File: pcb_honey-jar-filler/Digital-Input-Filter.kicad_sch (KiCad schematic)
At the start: 3 parts

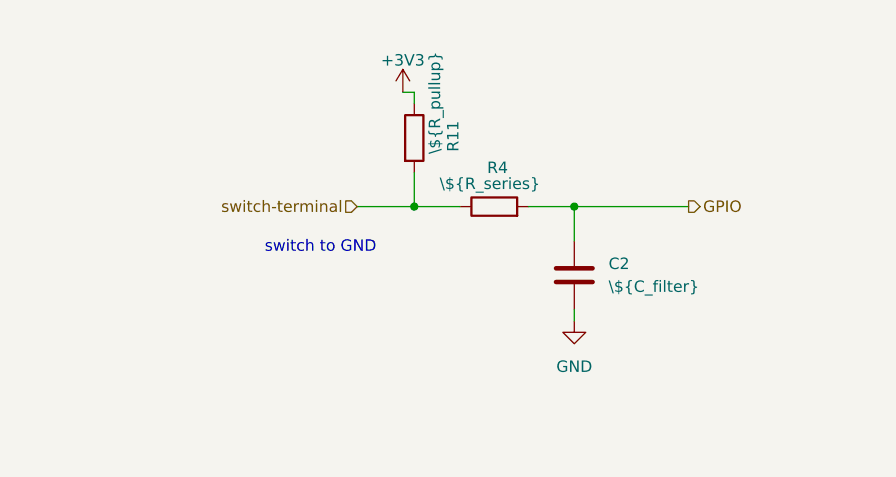
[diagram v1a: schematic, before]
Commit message: PCB: Optimize schematic layout, Add thesis schematic version
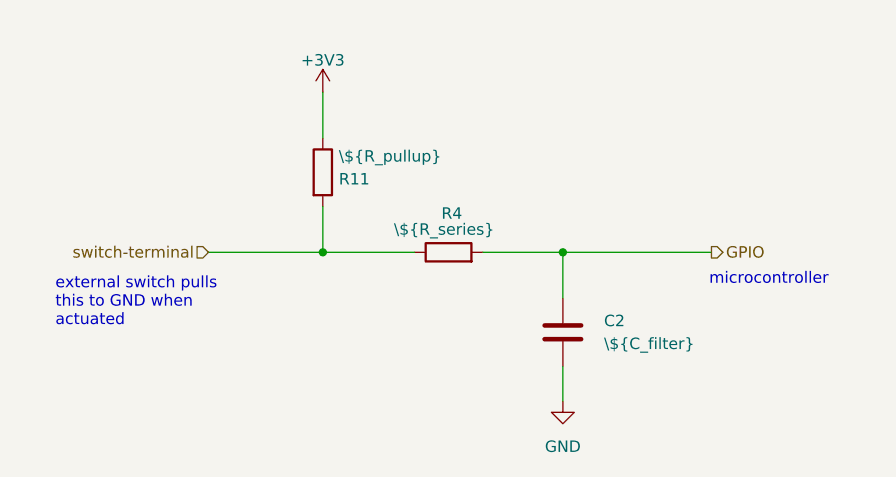
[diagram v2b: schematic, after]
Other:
- note added: "external switch pulls this to GND when actuated"
- note added: "microcontroller"
- note removed: "switch to GND"
- title: (none) -> Digital-Input-Filter
- moved on the sheet: C2, R11, R4
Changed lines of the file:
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@@
 	(generator "eeschema")
 	(generator_version "10.0")
-	(paper "A4")
-	(text "switch to GND"
-		(exclude_from_sim no)
-		(at 54.356 41.402 0)
+	(paper "A5")
+	(title_block
+		(title "Digital-Input-Filter")
+		(comment 1 "schematic component re-used for multiple inputs")
+	)
+	(text "microcontroller"
+		(exclude_from_sim no)
+		(at 97.536 44.958 0)
 		(effects
 			(font
 				(size 1.27 1.27)
 			)
-		)
-	)
-	(junction
-		(at 64.77 36.83)
-		(diameter 0)
-		(color 0 0 0 0)
-	)
-	(junction
-		(at 82.55 36.83)
-		(diameter 0)
-		(color 0 0 0 0)
-	)
-	(wire
-		(pts
-			(xy 58.42 36.83) (xy 64.77 36.83)
-		)
-		(stroke
-			(width 0)
-			(type default)
-		)
-	)
-	(wire
-		(pts
-			(xy 64.77 36.83) (xy 69.85 36.83)
-		)
-		(stroke
-			(width 0)
-			(type default)
-		)
-	)
-	(wire
-		(pts
-			(xy 77.47 36.83) (xy 82.55 36.83)
-		)
-		(stroke
-			(width 0)
-			(type default)
-		)
-	)
-	(wire
-		(pts
-			(xy 64.77 33.02) (xy 64.77 36.83)
-		)
-		(stroke
-			(width 0)
-			(type default)
-		)
-	)
-	(wire
-		(pts
-			(xy 82.55 48.26) (xy 82.55 49.53)
-		)
-		(stroke
-			(width 0)
-			(type default)
-		)
-	)
-	(wire
-		(pts
-			(xy 64.77 24.13) (xy 63.5 24.13)
-		)
-		(stroke
-			(width 0)
-			(type default)
-		)
-	)
-	(wire
-		(pts
-			(xy 82.55 36.83) (xy 95.25 36.83)
-		)
-		(stroke
-			(width 0)
-			(type default)
-		)
-	)
-	(wire
-		(pts
-			(xy 64.77 24.13) (xy 64.77 25.4)
-		)
-		(stroke
-			(width 0)
-			(type default)
-		)
-	)
-	(wire
-		(pts
-			(xy 82.55 36.83) (xy 82.55 40.64)
-		)
-		(stroke
-			(width 0)
-			(type default)
-		)
-	)
-	(hierarchical_label "GPIO"
-		(shape output)
-		(at 95.25 36.83 0)
+			(justify left)
+		)
+	)
+	(text "external switch pulls\nthis to GND when\nactuated"
+		(exclude_from_sim no)
+		(at 24.892 47.498 0)
 		(effects
 			(font
@@
 		)
 	)
-	(hierarchical_label "switch-terminal"
-		(shape input)
-		(at 58.42 36.83 180)
+	(junction
+		(at 54.61 41.91)
+		(diameter 0)
+		(color 0 0 0 0)
+	)
+	(junction
+		(at 81.28 41.91)
+		(diameter 0)
+		(color 0 0 0 0)
+	)
+	(wire
+		(pts
+			(xy 41.91 41.91) (xy 54.61 41.91)
+		)
+		(stroke
+			(width 0)
+			(type default)
+		)
+	)
+	(wire
+		(pts
+			(xy 72.39 41.91) (xy 81.28 41.91)
+		)
+		(stroke
+			(width 0)
+			(type default)
+		)
+	)
+	(wire
+		(pts
+			(xy 54.61 36.83) (xy 54.61 41.91)
+		)
+		(stroke
+			(width 0)
+			(type default)
+		)
+	)
+	(wire
+		(pts
+			(xy 81.28 54.61) (xy 81.28 58.42)
+		)
+		(stroke
+			(width 0)
+			(type default)
+		)
+	)
+	(wire
+		(pts
+			(xy 54.61 41.91) (xy 64.77 41.91)
+		)
+		(stroke
+			(width 0)
+			(type default)
+		)
+	)
+	(wire
+		(pts
+			(xy 81.28 41.91) (xy 97.79 41.91)
+		)
+		(stroke
+			(width 0)
+			(type default)
+		)
+	)
+	(wire
+		(pts
+			(xy 54.61 24.13) (xy 54.61 29.21)
+		)
+		(stroke
+			(width 0)
+			(type default)
+		)
+	)
+	(wire
+		(pts
+			(xy 81.28 41.91) (xy 81.28 46.99)
+		)
+		(stroke
+			(width 0)
+			(type default)
+		)
+	)
+	(hierarchical_label "GPIO"
+		(shape output)
+		(at 97.79 41.91 0)
 		(effects
 			(font
 				(size 1.27 1.27)
 			)
+			(justify left)
+		)
+	)
+	(hierarchical_label "switch-terminal"
+		(shape input)
+		(at 41.91 41.91 180)
+		(effects
+			(font
+				(size 1.27 1.27)
+			)
 			(justify right)
 		)
@@
 	(symbol
 		(lib_id "Device:C")
-		(at 82.55 44.45 0)
+		(at 81.28 50.8 0)
 		(unit 1)
 		(body_style 1)
@@
 		(in_pos_files yes)
 		(dnp no)
-		(fields_autoplaced yes)
 		(property "Reference" "C2"
-			(at 86.36 43.1799 0)
+			(at 85.852 49.53 0)
 			(show_name no)
 			(do_not_autoplace no)
@@
 		)
 		(property "Value" "\\${C_filter}"
-			(at 86.36 45.7199 0)
+			(at 85.852 52.07 0)
 			(show_name no)
 			(do_not_autoplace no)
@@
 		)
 		(property "Footprint" "capacitor_libJonny:C_DualType__Disc-7.0x2.5mm-P5mm__Elko-D5mm-P2.5mm"
-			(at 83.5152 48.26 0)
+			(at 82.2452 54.61 0)
 			(hide yes)
 			(show_name no)
@@
 		)
 		(property "Datasheet" ""
-			(at 82.55 44.45 0)
+			(at 81.28 50.8 0)
 			(hide yes)
 			(show_name no)
@@
 		)
 		(property "Description" "Unpolarized capacitor"
-			(at 82.55 44.45 0)
+			(at 81.28 50.8 0)
 			(hide yes)
 			(show_name no)
@@
 		)
 		(instances
-			(project "pcb_honey-jar-filler"
+			(project "pcb_honey-jar-filler_THESIS"
 				(path "/a100c00b-2f77-4961-b47b-c97e134b1df6/01ec2f49-36ac-41b2-8359-608f58bb2dcf"
 					(reference "C2")
@@
 	(symbol
 		(lib_id "power:+3V3")
-		(at 63.5 24.13 0)
+		(at 54.61 24.13 0)
 		(unit 1)
 		(body_style 1)
@@
 		(dnp no)
 		(property "Reference" "#PWR050"
-			(at 63.5 27.94 0)
+			(at 54.61 27.94 0)
 			(hide yes)
 			(show_name no)
@@
 		)
 		(property "Value" "+3V3"
-			(at 63.5 20.574 0)
+			(at 54.61 20.574 0)
 			(show_name no)
 			(do_not_autoplace no)
@@
 		)
 		(property "Footprint" ""
-			(at 63.5 24.13 0)
+			(at 54.61 24.13 0)
 			(hide yes)
 			(show_name no)
@@
 		)
 		(property "Datasheet" ""
-			(at 63.5 24.13 0)
+			(at 54.61 24.13 0)
 			(hide yes)
 			(show_name no)
@@
 		)
 		(property "Description" "Power symbol creates a global label with name \"+3V3\""
-			(at 63.5 24.13 0)
+			(at 54.61 24.13 0)
 			(hide yes)
 			(show_name no)
@@
 		)
 		(instances
-			(project "pcb_honey-jar-filler"
+			(project "pcb_honey-jar-filler_THESIS"
 				(path "/a100c00b-2f77-4961-b47b-c97e134b1df6/01ec2f49-36ac-41b2-8359-608f58bb2dcf"
 					(reference "#PWR050")
@@
 	(symbol
 		(lib_id "Device:R")
-		(at 73.66 36.83 90)
+		(at 68.58 41.91 90)
 		(unit 1)
 		(body_style 1)
@@
 		(dnp no)
 		(property "Reference" "R4"
-			(at 75.184 32.512 90)
+			(at 70.104 37.592 90)
 			(show_name no)
 			(do_not_autoplace no)
@@
 		)
 		(property "Value" "\\${R_series}"
-			(at 78.74 34.29 90)
+			(at 73.66 39.37 90)
 			(show_name no)
 			(do_not_autoplace no)
@@
 		)
 		(property "Footprint" "Resistor_THT:R_Axial_DIN0207_L6.3mm_D2.5mm_P10.16mm_Horizontal"
-			(at 73.66 38.608 90)
+			(at 68.58 43.688 90)
 			(hide yes)
 			(show_name no)
@@
 		)
 		(property "Datasheet" ""
-			(at 73.66 36.83 0)
+			(at 68.58 41.91 0)
 			(hide yes)
 			(show_name no)
@@
 		)
 		(property "Description" "Resistor"
-			(at 73.66 36.83 0)
+			(at 68.58 41.91 0)
 			(hide yes)
 			(show_name no)
@@
 		)
 		(instances
-			(project "pcb_honey-jar-filler"
+			(project "pcb_honey-jar-filler_THESIS"
 				(path "/a100c00b-2f77-4961-b47b-c97e134b1df6/01ec2f49-36ac-41b2-8359-608f58bb2dcf"
 					(reference "R4")
@@
 	(symbol
 		(lib_id "power:GND")
-		(at 82.55 49.53 0)
+		(at 81.28 58.42 0)
 		(unit 1)
 		(body_style 1)
@@
 		(fields_autoplaced yes)
 		(property "Reference" "#PWR027"
-			(at 82.55 55.88 0)
+			(at 81.28 64.77 0)
 			(hide yes)
 			(show_name no)
@@
 		)
 		(property "Value" "GND"
-			(at 82.55 54.61 0)
+			(at 81.28 63.5 0)
 			(show_name no)
 			(do_not_autoplace no)
@@
 		)
 		(property "Footprint" ""
-			(at 82.55 49.53 0)
+			(at 81.28 58.42 0)
 			(hide yes)
 			(show_name no)
@@
 		)
 		(property "Datasheet" ""
-			(at 82.55 49.53 0)
+			(at 81.28 58.42 0)
 			(hide yes)
 			(show_name no)
@@
 		)
 		(property "Description" "Power symbol creates a global label with name \"GND\" , ground"
-			(at 82.55 49.53 0)
+			(at 81.28 58.42 0)
 			(hide yes)
 			(show_name no)
@@
 		)
 		(instances
-			(project "pcb_honey-jar-filler"
+			(project "pcb_honey-jar-filler_THESIS"
 				(path "/a100c00b-2f77-4961-b47b-c97e134b1df6/01ec2f49-36ac-41b2-8359-608f58bb2dcf"
 					(reference "#PWR027")
@@
 	(symbol
 		(lib_id "Device:R")
-		(at 64.77 29.21 0)
+		(at 54.61 33.02 0)
 		(unit 1)
 		(body_style 1)
@@
 		(dnp no)
 		(property "Reference" "R11"
-			(at 69.088 30.734 90)
+			(at 56.388 33.782 0)
 			(show_name no)
 			(do_not_autoplace no)
@@
 		)
 		(property "Value" "\\${R_pullup}"
-			(at 67.056 30.988 90)
+			(at 56.388 31.242 0)
 			(show_name no)
 			(do_not_autoplace no)
@@
 		)
 		(property "Footprint" "Resistor_THT:R_Axial_DIN0207_L6.3mm_D2.5mm_P10.16mm_Horizontal"
-			(at 62.992 29.21 90)
+			(at 52.832 33.02 90)
 			(hide yes)
 			(show_name no)
@@
 		)
 		(property "Datasheet" ""
-			(at 64.77 29.21 0)
+			(at 54.61 33.02 0)
 			(hide yes)
 			(show_name no)
@@
 		)
 		(property "Description" "Resistor"
-			(at 64.77 29.21 0)
+			(at 54.61 33.02 0)
 			(hide yes)
 			(show_name no)
@@
 		)
 		(instances
-			(project "pcb_honey-jar-filler"
+			(project "pcb_honey-jar-filler_THESIS"
 				(path "/a100c00b-2f77-4961-b47b-c97e134b1df6/01ec2f49-36ac-41b2-8359-608f58bb2dcf"
 					(reference "R11")
